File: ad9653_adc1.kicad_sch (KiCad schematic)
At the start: 20 parts, among them J701 142-0701-201, J702 142-0701-201, J703 142-0701-201, J704 142-0701-201, U701 AD9653BCPZ-125

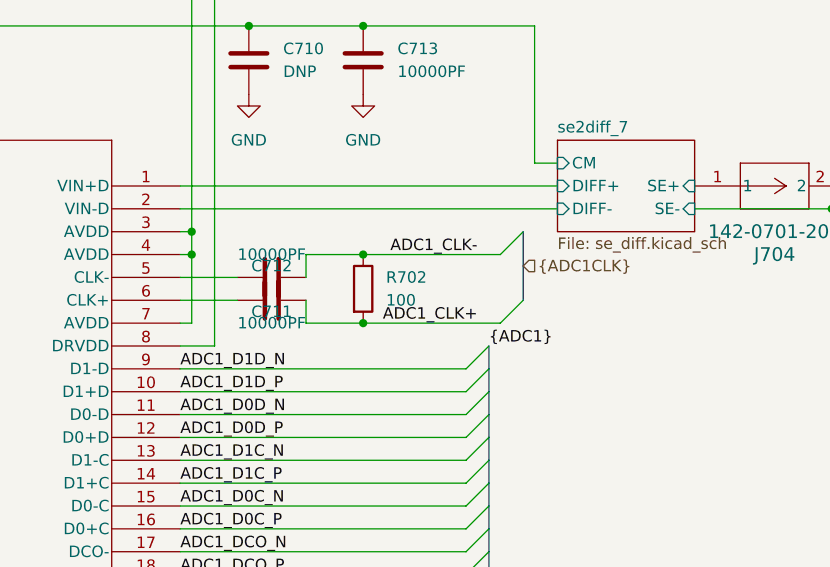
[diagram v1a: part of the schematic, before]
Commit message: fixed differential pair impedance and length matching. Also fixed DRC errors (trace spacing). These are only layout changes, the schematic remains unchanged.
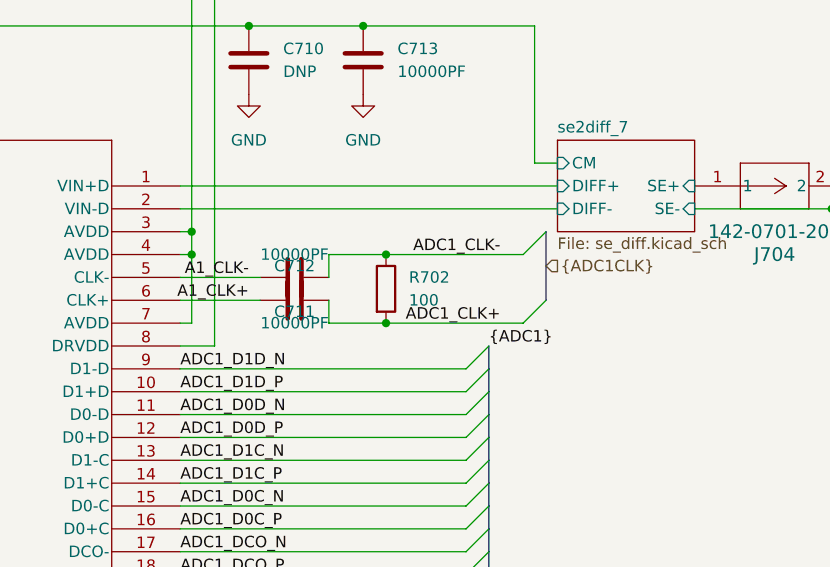
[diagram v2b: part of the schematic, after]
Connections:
- net A1_CLK-: now reaches C711.2, U701.5 (CLK-)
- net A1_CLK+: now reaches C712.2, U701.6 (CLK+)
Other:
- moved on the sheet: C711, C712, R702
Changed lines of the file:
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@@
 	)
 	(junction
-		(at 219.71 102.87)
+		(at 222.25 102.87)
 		(diameter 0)
 		(color 0 0 0 0)
@@
 	)
 	(junction
-		(at 219.71 95.25)
+		(at 222.25 95.25)
 		(diameter 0)
 		(color 0 0 0 0)
@@
 	)
 	(bus_entry
-		(at 237.49 100.33)
+		(at 240.03 100.33)
 		(size -2.54 2.54)
 		(stroke
@@
 	)
 	(bus_entry
-		(at 237.49 92.71)
+		(at 240.03 92.71)
 		(size -2.54 2.54)
 		(stroke
@@
 	(wire
 		(pts
-			(xy 199.39 100.33) (xy 205.74 100.33)
+			(xy 199.39 100.33) (xy 208.28 100.33)
 		)
 		(stroke
@@
 	(wire
 		(pts
-			(xy 213.36 100.33) (xy 213.36 102.87)
+			(xy 215.9 100.33) (xy 215.9 102.87)
 		)
 		(stroke
@@
 	(wire
 		(pts
-			(xy 213.36 97.79) (xy 213.36 95.25)
+			(xy 215.9 97.79) (xy 215.9 95.25)
 		)
 		(stroke
@@
 	(bus
 		(pts
-			(xy 237.49 92.71) (xy 237.49 100.33)
+			(xy 240.03 92.71) (xy 240.03 100.33)
 		)
 		(stroke
@@
 	(wire
 		(pts
-			(xy 219.71 102.87) (xy 234.95 102.87)
+			(xy 222.25 102.87) (xy 237.49 102.87)
 		)
 		(stroke
@@
 	(wire
 		(pts
-			(xy 213.36 102.87) (xy 219.71 102.87)
+			(xy 215.9 102.87) (xy 222.25 102.87)
 		)
 		(stroke
@@
 	(wire
 		(pts
-			(xy 199.39 97.79) (xy 205.74 97.79)
+			(xy 199.39 97.79) (xy 208.28 97.79)
 		)
 		(stroke
@@
 	(wire
 		(pts
-			(xy 219.71 95.25) (xy 234.95 95.25)
+			(xy 222.25 95.25) (xy 237.49 95.25)
 		)
 		(stroke
@@
 	(wire
 		(pts
-			(xy 213.36 95.25) (xy 219.71 95.25)
+			(xy 215.9 95.25) (xy 222.25 95.25)
 		)
 		(stroke
@@
 		)
 	)
+	(label "A1_CLK-"
+		(at 207.01 97.79 180)
+		(effects
+			(font
+				(size 1.27 1.27)
+			)
+			(justify right bottom)
+		)
+	)
+	(label "A1_CLK+"
+		(at 207.01 100.33 180)
+		(effects
+			(font
+				(size 1.27 1.27)
+			)
+			(justify right bottom)
+		)
+	)
 	(label "ADC1_CLK-"
-		(at 232.41 95.25 180)
+		(at 234.95 95.25 180)
 		(effects
 			(font
@@
 	)
 	(label "ADC1_CLK+"
-		(at 232.41 102.87 180)
+		(at 234.95 102.87 180)
 		(effects
 			(font
@@
 	(hierarchical_label "{ADC1CLK}"
 		(shape input)
-		(at 237.49 96.52 0)
+		(at 240.03 96.52 0)
 		(effects
 			(font
@@
 	(symbol
 		(lib_id "Device:R")
-		(at 219.71 99.06 0)
+		(at 222.25 99.06 0)
 		(unit 1)
 		(body_style 1)
@@
 		(fields_autoplaced yes)
 		(property "Reference" "R702"
-			(at 222.25 97.7899 0)
+			(at 224.79 97.7899 0)
 			(show_name no)
 			(do_not_autoplace no)
@@
 		)
 		(property "Value" "100"
-			(at 222.25 100.3299 0)
+			(at 224.79 100.3299 0)
 			(show_name no)
 			(do_not_autoplace no)
@@
 		)
 		(property "Footprint" "Resistor_SMD:R_0603_1608Metric"
-			(at 217.932 99.06 90)
+			(at 220.472 99.06 90)
 			(hide yes)
 			(show_name no)
@@
 		)
 		(property "Datasheet" ""
-			(at 219.71 99.06 0)
+			(at 222.25 99.06 0)
 			(hide yes)
 			(show_name no)
@@
 		)
 		(property "Description" "Resistor"
-			(at 219.71 99.06 0)
+			(at 222.25 99.06 0)
 			(hide yes)
 			(show_name no)
@@
 		)
 		(property "Vendor" "digikey:311-100HRCT-ND"
-			(at 0 198.12 0)
+			(at 2.54 198.12 0)
 			(hide yes)
 			(show_name no)
@@
 	(symbol
 		(lib_id "Device:C")
-		(at 209.55 100.33 270)
+		(at 212.09 100.33 270)
 		(mirror x)
 		(unit 1)
@@
 		(dnp no)
 		(property "Reference" "C712"
-			(at 209.55 96.52 90)
+			(at 212.09 96.52 90)
 			(show_name no)
 			(do_not_autoplace no)
@@
 		)
 		(property "Value" "10000PF"
-			(at 209.55 95.25 90)
+			(at 212.09 95.25 90)
 			(show_name no)
 			(do_not_autoplace no)
@@
 		)
 		(property "Footprint" "Capacitor_SMD:C_0603_1608Metric"
-			(at 205.74 99.3648 0)
+			(at 208.28 99.3648 0)
 			(hide yes)
 			(show_name no)
@@
 		)
 		(property "Datasheet" ""
-			(at 209.55 100.33 0)
+			(at 212.09 100.33 0)
 			(hide yes)
 			(show_name no)
@@
 		)
 		(property "Description" "Unpolarized capacitor"
-			(at 209.55 100.33 0)
+			(at 212.09 100.33 0)
 			(hide yes)
 			(show_name no)
@@
 		)
 		(property "Vendor" "digikey:445-2664-1-ND"
-			(at 109.22 309.88 0)
+			(at 111.76 309.88 0)
 			(hide yes)
 			(show_name no)
@@
 	(symbol
 		(lib_id "Device:C")
-		(at 209.55 97.79 270)
+		(at 212.09 97.79 270)
 		(unit 1)
 		(body_style 1)
@@
 		(dnp no)
 		(property "Reference" "C711"
-			(at 209.55 101.6 90)
+			(at 212.09 101.6 90)
 			(show_name no)
 			(do_not_autoplace no)
@@
 		)
 		(property "Value" "10000PF"
-			(at 209.55 102.87 90)
+			(at 212.09 102.87 90)
 			(show_name no)
 			(do_not_autoplace no)
@@
 		)
 		(property "Footprint" "Capacitor_SMD:C_0603_1608Metric"
-			(at 205.74 98.7552 0)
+			(at 208.28 98.7552 0)
 			(hide yes)
 			(show_name no)
@@
 		)
 		(property "Datasheet" ""
-			(at 209.55 97.79 0)
+			(at 212.09 97.79 0)
 			(hide yes)
 			(show_name no)
@@
 		)
 		(property "Description" "Unpolarized capacitor"
-			(at 209.55 97.79 0)
+			(at 212.09 97.79 0)
 			(hide yes)
 			(show_name no)
@@
 		)
 		(property "Vendor" "digikey:445-2664-1-ND"
-			(at 111.76 -111.76 0)
+			(at 114.3 -111.76 0)
 			(hide yes)
 			(show_name no)
